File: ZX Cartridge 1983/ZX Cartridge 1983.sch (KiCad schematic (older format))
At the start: 18 parts, among them J1 Cartridge, M1 Mounting, M2 Mounting, M3 Mounting, M4 Mounting, SW1 ROM_SEL, U1 27C020, U2 MC14495P1

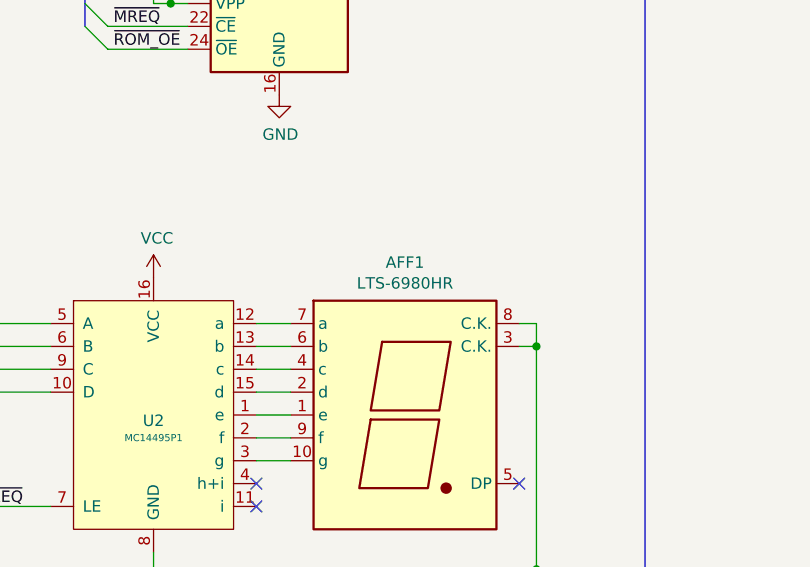
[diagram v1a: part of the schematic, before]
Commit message: Silkscreen tweaks
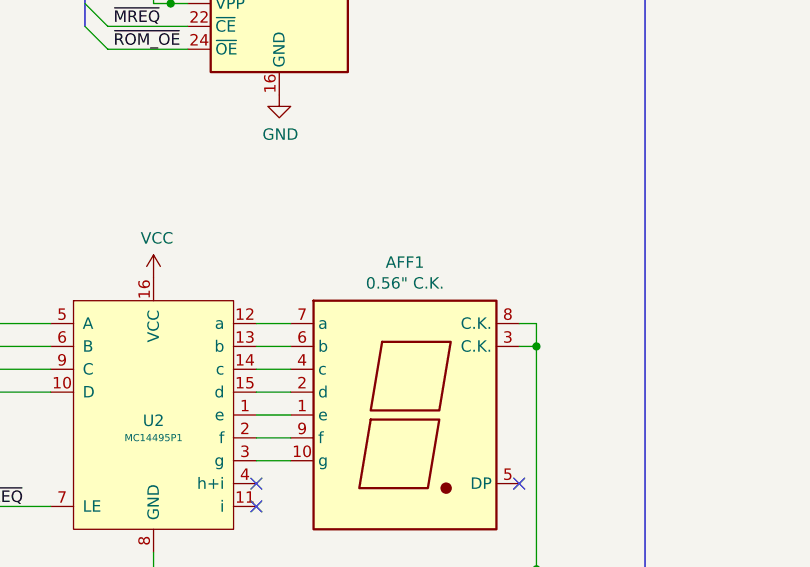
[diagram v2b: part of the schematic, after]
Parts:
- AFF1: value LTS-6980HR -> 0.56\" C.K.
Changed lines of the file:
@@
 P 6500 4975
 F 0 "AFF1" H 6500 5642 50  0000 C CNN
-F 1 "LTS-6980HR" H 6500 5551 50  0000 C CNN
+F 1 "0.56\" C.K." H 6500 5551 50  0000 C CNN
 F 2 "Display_7Segment:7SegmentLED_LTS6760_LTS6780" H 6500 4375 50  0001 C CNN
 F 3 "http://datasheet.octopart.com/LTS-6960HR-Lite-On-datasheet-11803242.pdf" H 6500 4975 50  0001 C CNN

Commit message: Marked pinouts for smaller chips
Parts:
- U1: footprint Package_DIP:DIP-32_W15.24mm_Socket_LongPads -> 27c020:DIP-32_W15.24mm_Socket_LongPads
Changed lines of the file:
@@
 F 0 "U1" H 5725 3525 50  0000 C CNN
 F 1 "27C020" V 5950 2275 50  0000 C CNN
-F 2 "Package_DIP:DIP-32_W15.24mm_Socket_LongPads" H 5950 2275 50  0001 C CNN
+F 2 "27c020:DIP-32_W15.24mm_Socket_LongPads" H 5950 2275 50  0001 C CNN
 F 3 "http://ww1.microchip.com/downloads/en/devicedoc/doc0570.pdf" H 5950 2275 50  0001 C CNN
 	1    5950 2275
